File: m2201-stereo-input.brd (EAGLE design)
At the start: 100 x 50 mm, 69 parts, among them U1 ERM1-5MM, U2 ERM1-5MM

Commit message: Add (dummy) FX2 connectors to sch
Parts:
- added U3: FX2-20P-1.27DS, hardware:EMPTY
- added U4: FX2-20S-1.27DS, hardware:EMPTY
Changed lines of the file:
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@@
 <attribute name="MOUSER" value="660-RK73H2ATTD1003F" x="51" y="32" size="0.8128" layer="27" ratio="15" rot="R90" display="off"/>
+</element>
+<element name="U3" library="hardware" package="EMPTY" value="FX2-20P-1.27DS" x="-60" y="-7">
+<attribute name="MOUSER" value="798-FX2-20P-1.27DS71" x="-60" y="-7" size="1.778" layer="27" display="off"/>
+</element>
+<element name="U4" library="hardware" package="EMPTY" value="FX2-20S-1.27DS" x="-61" y="-9">
+<attribute name="MOUSER" value="798-FX2-20S-1.27DS71" x="-61" y="-9" size="1.778" layer="27" display="off"/>
 </element>
 </elements>

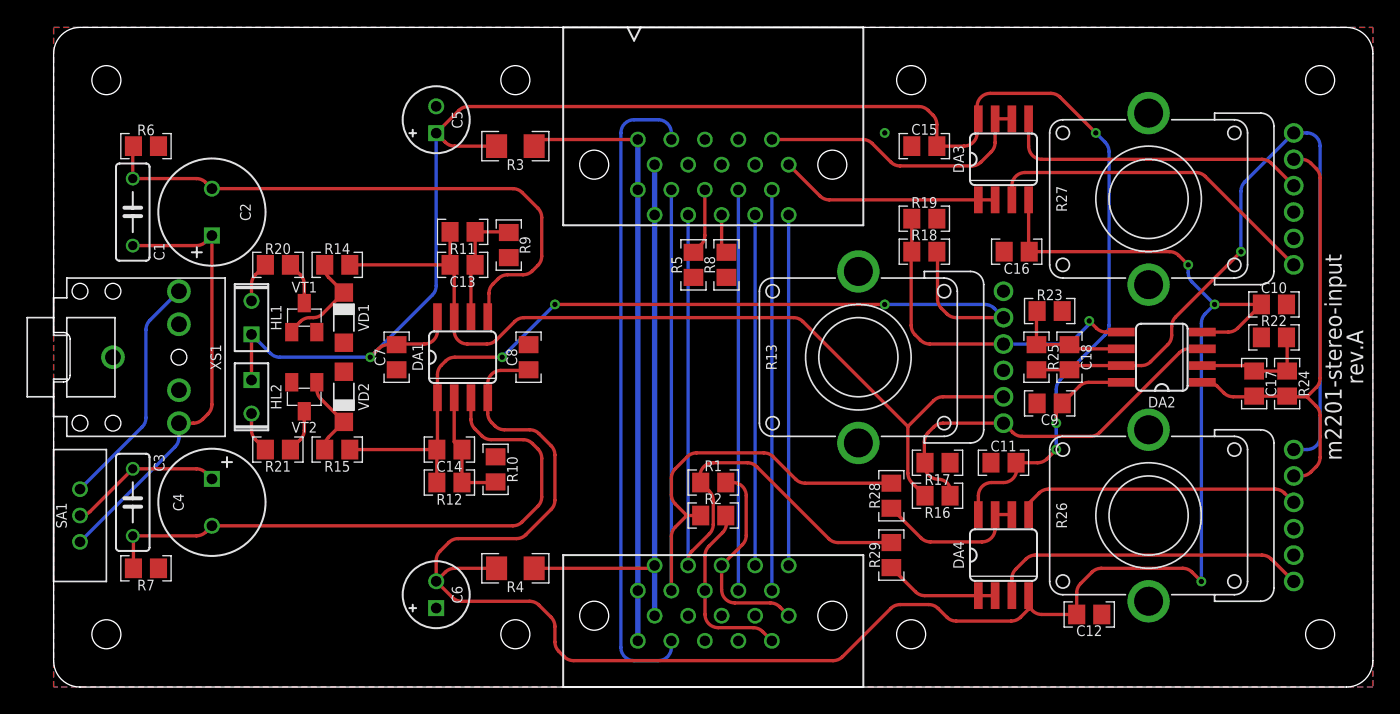
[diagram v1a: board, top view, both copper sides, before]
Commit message: Signal indicator refactoring (#5) + no noise when no jack inserted (#6)
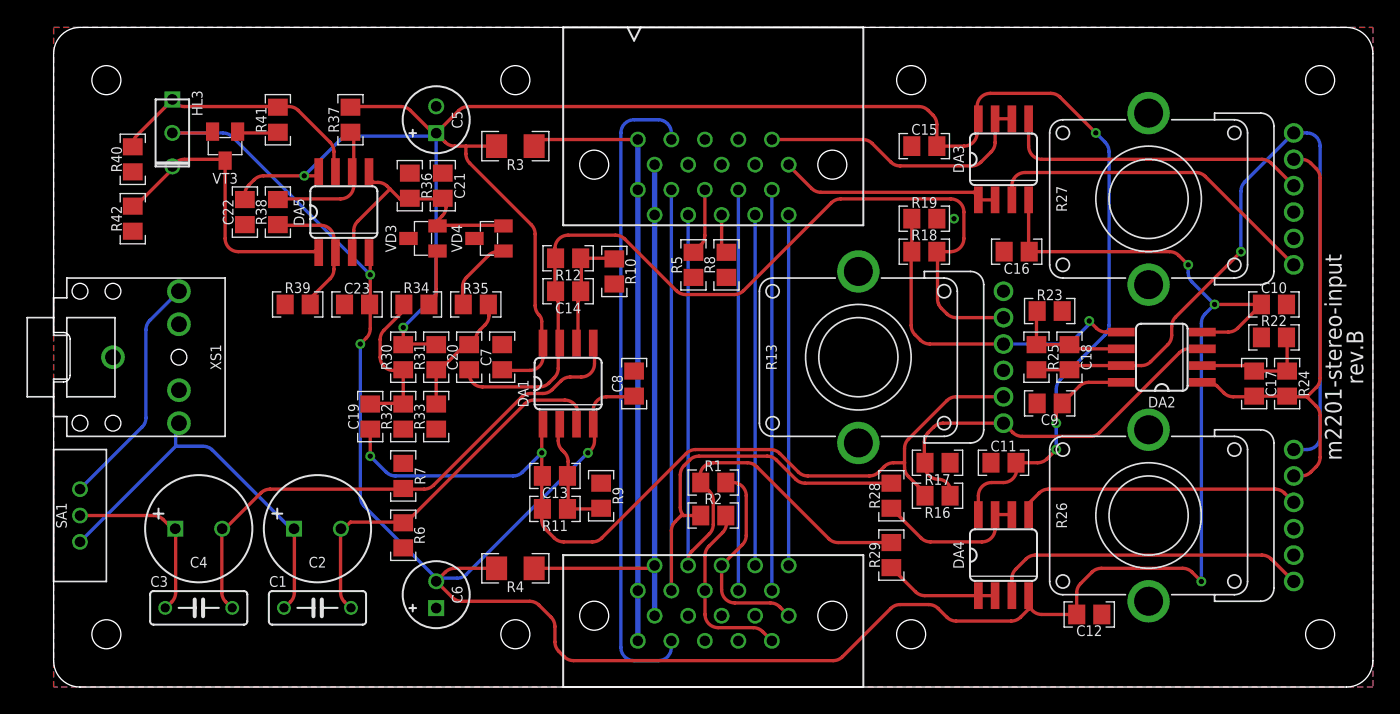
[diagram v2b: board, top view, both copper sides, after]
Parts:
- removed HL1, HL2: BLUE(2MMX5MM), optoelectronics:LED2X5
- removed R14, R15: 100K, resistors:R-0805
- removed R20, R21: 680R, resistors:R-0805
- removed U2: ERM1-5MM, hardware:EMPTY
- removed VD1, VD2: MMSD4148, diodes:SOD123
- removed VT1, VT2: BC848, transistors-npn:SOT23
- added C19, C20, C21, C22, C23: 100N, capacitors:C-0805
- added DA5: LM2903M, ic-fairchild:SO-8
- added HL3: RED/BLUE(2MMX5MM,CC), optoelectronics:LED2X5-3PIN
- added R30, R31: 10M, resistors:R-0805
- added R32, R33: 100K, resistors:R-0805
- added R34, R35: 47K, resistors:R-0805
- added R36: 330K, resistors:R-0805
- added R37: 22K, resistors:R-0805
- added R38: 4K7, resistors:R-0805
- added R39: 100R, resistors:R-0805
- added R40: 2K2, resistors:R-0805
- added R41: 10K, resistors:R-0805
- added R42: 1K8, resistors:R-0805
- added VD3, VD4: BAS16, diodes:SOT23
- added VT3: BC848, transistors-npn:SOT23
- PCB1: value rev.A -> rev.B
- moved R6 35.4 mm to (26.5, 11.5), turned to 90 degrees
- moved C1 33.1 mm to (20.0, 6.00), turned to 0 degrees
- moved C2 25.3 mm to (20.0, 12.0), turned to 0 degrees
- moved R11 22.1 mm to (38.0, 13.5)
- moved R7 20.7 mm to (26.5, 16.0), turned to 270 degrees
- moved R9 20.2 mm to (41.5, 14.5), turned to 270 degrees
- moved R12 19.2 mm to (39.0, 32.5)
- moved R10 17.5 mm to (42.5, 31.5), turned to 90 degrees
- moved C13 17.5 mm to (38.0, 16.0)
- moved C14 15.0 mm to (39.0, 30.0)
- moved C3 9.43 mm to (11.0, 6.00), turned to 0 degrees
- moved C8 8.25 mm to (44.0, 23.0)
- moved DA1 8.25 mm to (39.0, 23.0)
- moved C7 8.00 mm to (34.0, 25.0), turned to 270 degrees
- moved C4 2.24 mm to (11.0, 12.0), turned to 0 degrees
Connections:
- removed net N$30: R15.2, VD2.C, VT2.1
- removed net N$32: R21.1, VT2.3
- removed net N$33: HL2.K, R21.2
- removed net N$34: R14.2, VD1.C, VT1.1
- removed net N$35: R20.1, VT1.3
- removed net N$37: HL1.K, R20.2
- new net N$17: C19.2, R30.1, R32.2, R34.1
- new net N$29: R34.2, VD3.1
- new net N$31: C20.2, R31.1, R33.2, R35.1
- new net N$44: R35.2, VD4.1
- new net N$45: C21.2, DA5.3, DA5.5, R36.2, VD3.2, VD4.2
- new net N$46: DA5.2, R38.1, R39.2
- new net N$47: DA5.6, R37.1, R38.2
- new net N$48: DA5.7, HL3.A1, R40.1, R41.2
- new net N$49: R41.1, VT3.1
- new net N$51: DA5.1, HL3.A2, R42.1, VT3.3
- net +15V: now also C22.2, DA5.8, R30.2, R31.2, R37.2; no longer HL1.A, HL2.A
- net -15V: now also C23.1, DA5.4, HL3.K, VT3.2
- net GND: now also C21.1, C22.1, C23.2, R32.1, R33.1, R36.1, R39.1, R40.2, R42.2, XS1.10, XS1.11; no longer VD1.A, VD2.A, VT1.2, VT2.2
- net N$10: now also DA1.3; no longer DA1.5
- net N$15: now also C20.1, DA1.7; no longer DA1.1, R15.1
- net N$19: now also C19.1, DA1.1; no longer DA1.7, R14.1
- net N$26: now also DA1.2; no longer DA1.6
- net N$27: now also DA1.6; no longer DA1.2
- net N$9: now also DA1.5; no longer DA1.3
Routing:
- net -15V: track 152.2 -> 196.6 mm, vias 3 -> 6
- net +15V: track 142.9 -> 171.9 mm, vias 4 -> 5
- net N$51: track 0.00 -> 22.6 mm
- net N$45: track 0.00 -> 21.2 mm
- net N$48: track 0.00 -> 20.3 mm
- net N$10: track 44.9 -> 29.6 mm
- net N$17: track 0.00 -> 12.0 mm
- net N$47: track 0.00 -> 10.9 mm
- net N$31: track 0.00 -> 10.6 mm
- net N$46: track 0.00 -> 10.5 mm
- net N$34: track 7.79 -> 0.00 mm
- net N$30: track 6.42 -> 0.00 mm
- net N$44: track 0.00 -> 5.72 mm
- net N$9: track 46.1 -> 41.1 mm
- net N$29: track 0.00 -> 4.87 mm
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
